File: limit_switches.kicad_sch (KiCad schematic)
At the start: 31 parts, among them J13 Conn_01x02_Pin, J14 Conn_01x02_Pin, J15 Conn_01x02_Pin, J16 Conn_01x02_Pin, J17 Conn_01x02_Pin, J18 Conn_01x02_Pin

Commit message: finished routing
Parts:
- removed C18, C20, C22: 1uF, Capacitor_SMD:C_0603_1608Metric_Pad1.08x0.95mm_HandSolder, symbol Device:C
- removed D11, D7, D9: 1N4148W, Diode_SMD:D_SOD-123, symbol Diode:1N4148W
- removed J13, J15, J17: Conn_01x02_Pin, Connector_JST:JST_EH_B2B-EH-A_1x02_P2.50mm_Vertical, symbol Connector:Conn_01x02_Pin
- removed R22, R26, R31: 10k, Resistor_SMD:R_0603_1608Metric_Pad0.98x0.95mm_HandSolder, symbol Device:R_US
- removed R24, R28, R33: 1k, Resistor_SMD:R_0603_1608Metric_Pad0.98x0.95mm_HandSolder, symbol Device:R_US
- renumbered C19 to C18, C21 to C19, D8 to D7, D10 to D8, J18 to J13, J16 to J15, R23 to R22, R25 to R23, R29 to R24, R27 to R25, R30 to R26, R32 to R27

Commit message: aaaaaaaaaaaaaaaaaa
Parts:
- C17, C18, C19: now left out of the parts list
- J13, J14, J15: LCSC (none) -> C265281
- R22, R25, R27: LCSC (none) -> C2907113
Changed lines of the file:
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@@
+			)
+		)
+		(property "LCSC" "C265281"
+			(at 66.04 82.55 0)
+			(effects
+				(font
+					(size 1.27 1.27)
+				)
+				(hide yes)
 			)
 		)
@@
 		(unit 1)
 		(exclude_from_sim no)
-		(in_bom yes)
+		(in_bom no)
 		(on_board yes)
 		(dnp no)
@@
 			)
 		)
+		(property "LCSC" "C265281"
+			(at 66.04 59.69 0)
+			(effects
+				(font
+					(size 1.27 1.27)
+				)
+				(hide yes)
+			)
+		)
 		(pin "2"
 		)
@@
 		(unit 1)
 		(exclude_from_sim no)
-		(in_bom yes)
+		(in_bom no)
 		(on_board yes)
 		(dnp no)
@@
 		(unit 1)
 		(exclude_from_sim no)
-		(in_bom yes)
+		(in_bom no)
 		(on_board yes)
 		(dnp no)
@@
 			)
 		)
-		(property "LCSC" ""
+		(property "LCSC" "C2907113"
 			(at 82.55 105.41 0)
 			(effects
@@
 			)
 		)
-		(property "LCSC" ""
+		(property "LCSC" "C2907113"
 			(at 82.55 59.69 0)
 			(effects
@@
 			)
 		)
-		(property "LCSC" ""
+		(property "LCSC" "C2907113"
 			(at 82.55 82.55 0)
 			(effects
@@
 			(at 66.04 105.41 0)
 			(effects
+				(font
+					(size 1.27 1.27)
+				)
+				(hide yes)
+			)
+		)
+		(property "LCSC" "C265281"
+			(at 66.04 105.41 0)
+			(effects

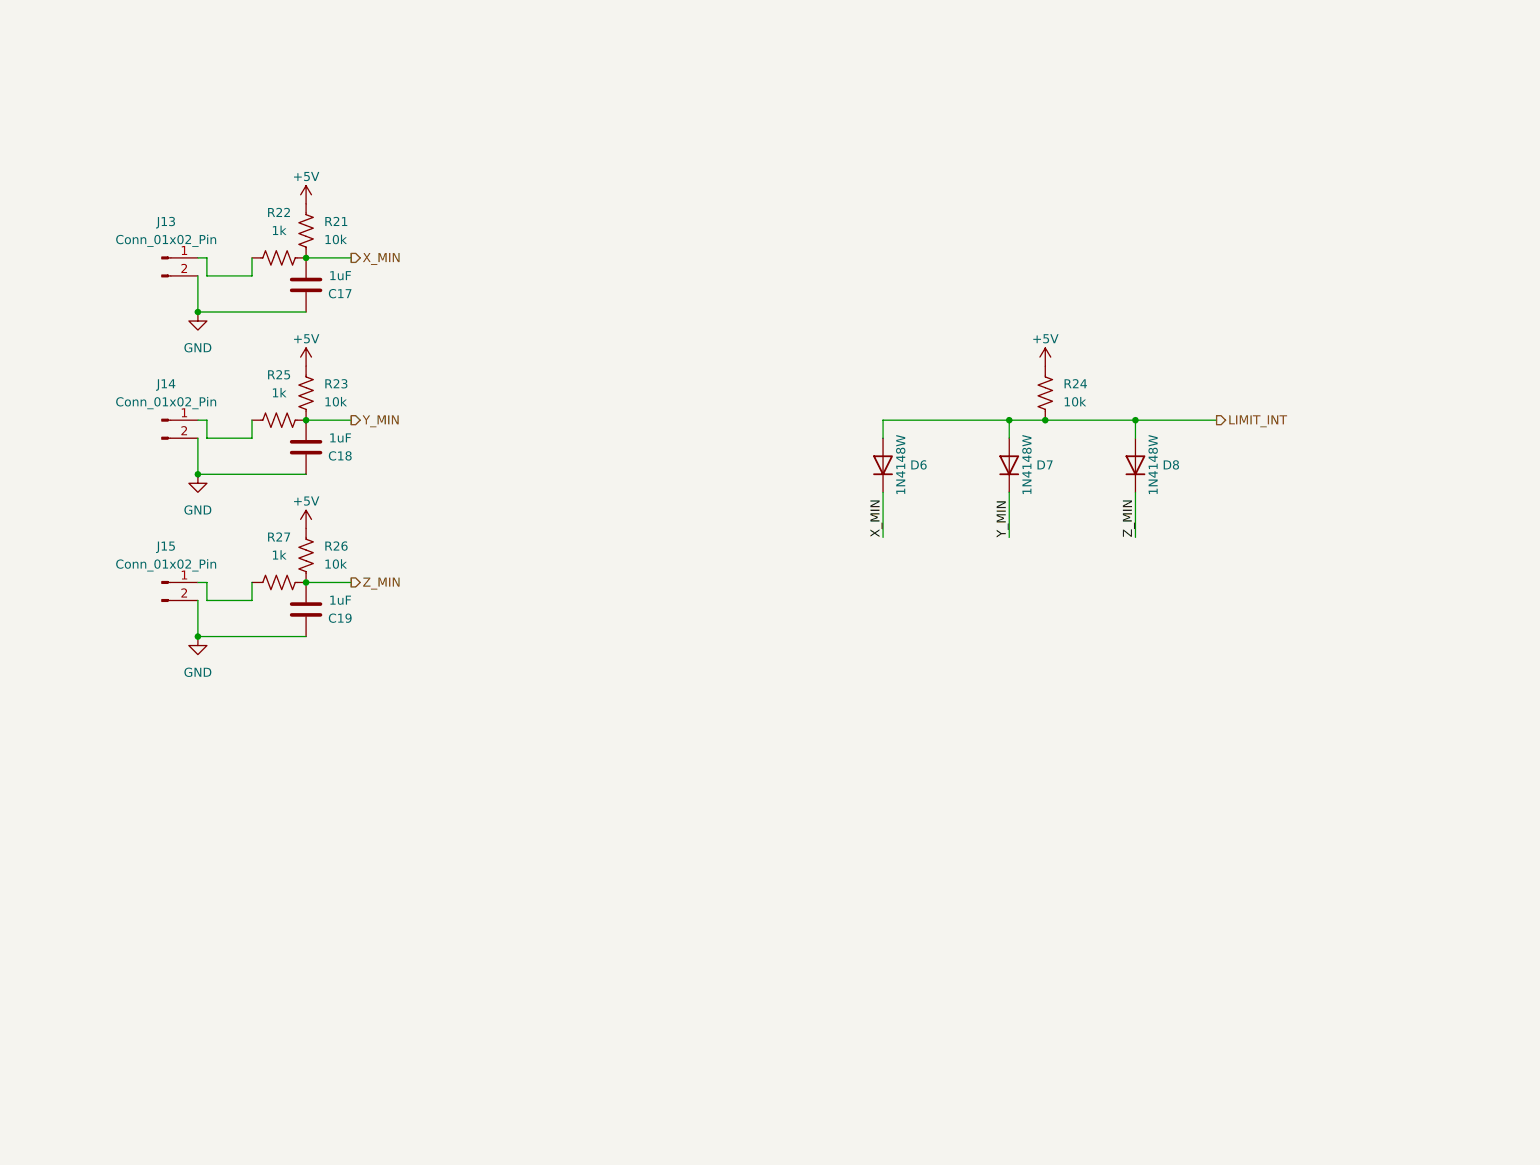
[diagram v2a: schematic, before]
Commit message: DXL Buffer circuit and new prod file
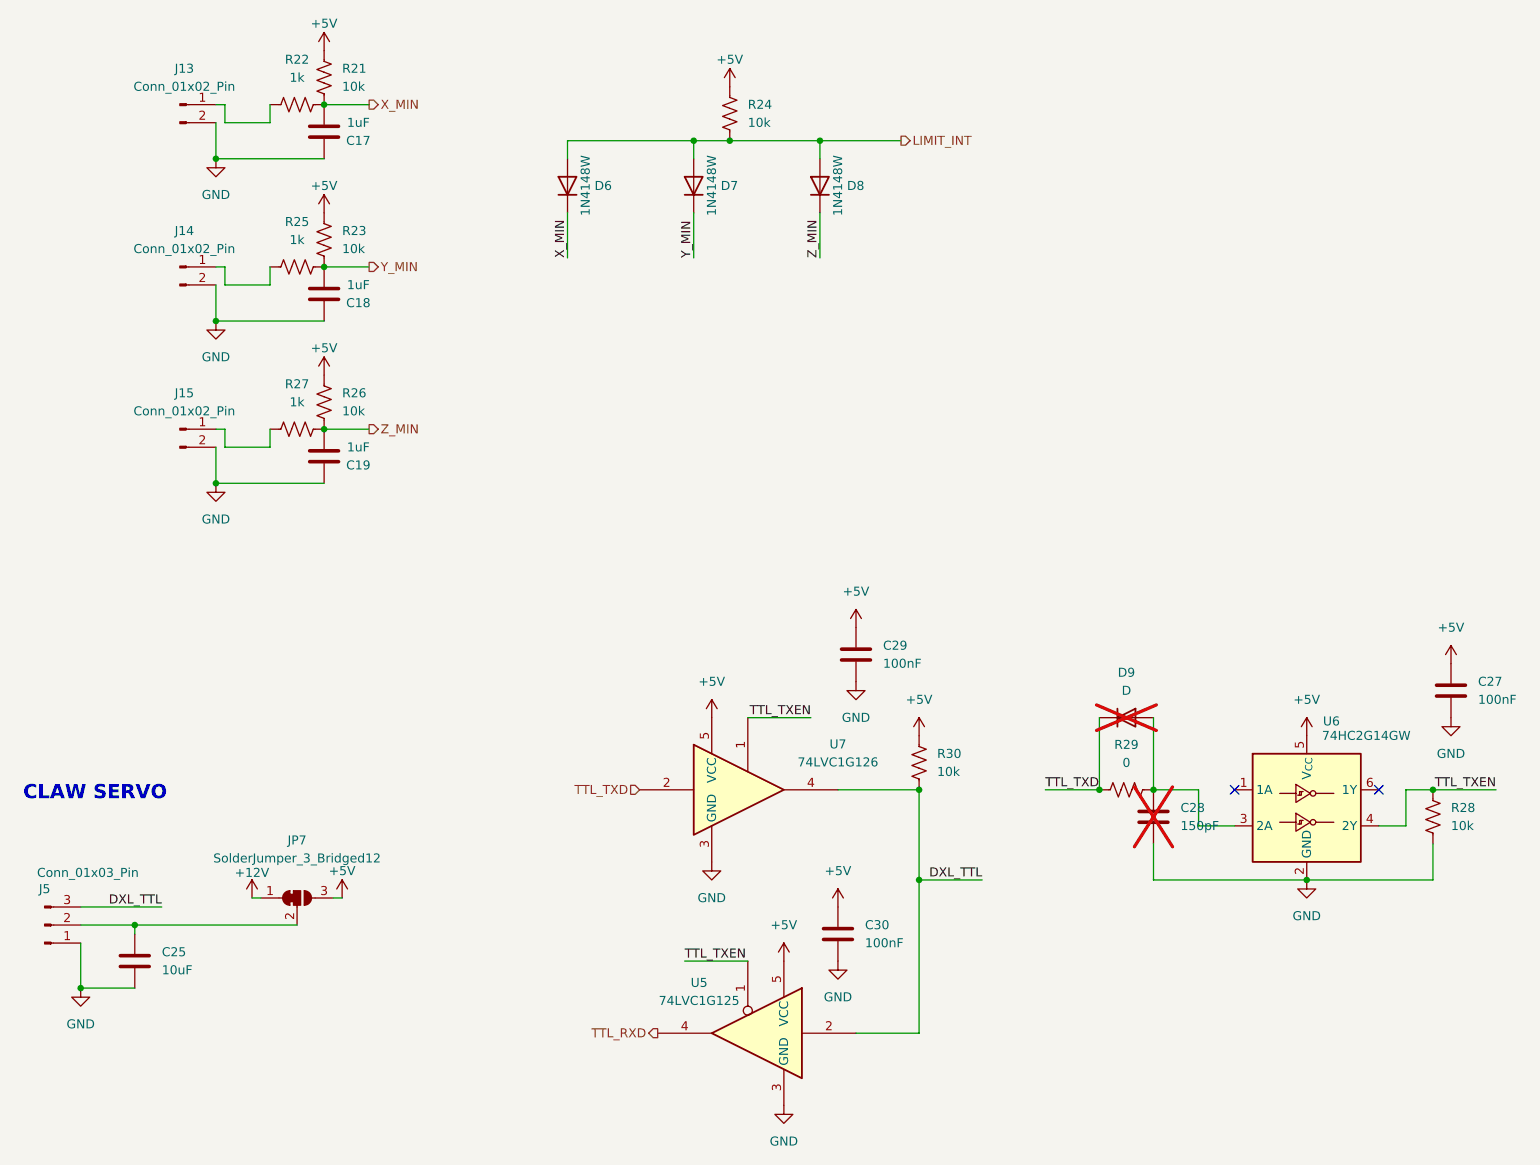
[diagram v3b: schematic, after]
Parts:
- added C25: 10uF, Capacitor_SMD:C_0805_2012Metric, symbol Device:C
- added C27, C29, C30: 100nF, Capacitor_SMD:C_0603_1608Metric_Pad1.08x0.95mm_HandSolder, symbol Device:C
- added C28: 150pF, Capacitor_SMD:C_0603_1608Metric_Pad1.08x0.95mm_HandSolder, symbol Device:C
- added D9: D, Diode_SMD:D_SOD-123, symbol Device:D
- added J5: Conn_01x03_Pin, Connector_JST:JST_EH_B3B-EH-A_1x03_P2.50mm_Vertical, symbol Connector:Conn_01x03_Pin
- added JP7: SolderJumper_3_Bridged12, Jumper:SolderJumper-3_P1.3mm_Bridged12_RoundedPad1.0x1.5mm, symbol Jumper:SolderJumper_3_Bridged12
- added R28, R30: 10k, Resistor_SMD:R_0603_1608Metric_Pad0.98x0.95mm_HandSolder, symbol Device:R_US
- added R29: 0, Resistor_SMD:R_0603_1608Metric_Pad0.98x0.95mm_HandSolder, symbol Device:R_US
- added U5: 74LVC1G125, Package_TO_SOT_SMD:SOT-353_SC-70-5, symbol 74xGxx:74LVC1G125
- added U6: 74HC2G14GW, Package_TO_SOT_SMD:SOT-363_SC-70-6, symbol 74xGxx:Inverter_Schmitt_Dual
- added U7: 74LVC1G126, Package_TO_SOT_SMD:SOT-353_SC-70-5, symbol 74xGxx:74LVC1G126
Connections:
- net +5V: now also C27.1, C29.1, C30.1, JP7.3 (B), R30.1, U5.5 (VCC), U6.5 (V_{CC}), U7.5 (VCC)
- net GND: now also C25.2, C27.2, C28.2, C29.2, C30.2, J5.1 (Pin_1), R28.2, U5.3 (GND), U6.2 (GND), U7.3 (GND)
- new net: C25.1, J5.2 (Pin_2), JP7.2 (C)
- new net: C28.1, D9.2 (A), R29.2, U6.3 (2A)
- new net +12V: JP7.1 (A)
- new net DXL_TTL: J5.3 (Pin_3), R30.2, U5.2, U7.4
- new net TTL_RXD: U5.4
- new net TTL_TXD: D9.1 (K), R29.1, U7.2
- new net TTL_TXEN: R28.1, U5.1, U6.4 (2Y), U7.1
- no-connect marks 0 -> 2
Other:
- note added: "CLAW SERVO"
- moved on the sheet: C17, C18, C19, D6, D7, D8, J13, J14, J15, R21, R22, R23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

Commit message: added html bom
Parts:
- C17, C18, C19, C27, C29, C30: now in the parts list
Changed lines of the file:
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@@
 		(unit 1)
 		(exclude_from_sim no)
-		(in_bom no)
+		(in_bom yes)
 		(on_board yes)
 		(dnp no)
@@
 		(unit 1)
 		(exclude_from_sim no)
-		(in_bom no)
+		(in_bom yes)
 		(on_board yes)
 		(dnp no)
@@
 		(unit 1)
 		(exclude_from_sim no)
-		(in_bom no)
+		(in_bom yes)
 		(on_board yes)
 		(dnp no)
@@
 		(unit 1)
 		(exclude_from_sim no)
-		(in_bom no)
+		(in_bom yes)
 		(on_board yes)
 		(dnp no)
@@
 		(unit 1)
 		(exclude_from_sim no)
-		(in_bom no)
+		(in_bom yes)
 		(on_board yes)
 		(dnp no)
@@
 		(unit 1)
 		(exclude_from_sim no)
-		(in_bom no)
-		(on_board yes)
-		(dnp no)
+		(in_bom yes)
+		(on_board yes)
+		(dnp no)
